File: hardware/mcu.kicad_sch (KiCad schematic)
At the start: 49 parts, among them J10 PRPC006SAAN-RC, J11 SBH11-NBPC-D05-SM-BK, J12 PRPC006SAAN-RC, J13 PRPC006SAAN-RC, J14 PRPC006SAAN-RC, J15 PRPC006SAAN-RC, J16 PRPC006SAAN-RC, J17 PRPC006SAAN-RC, J18 PRPC001DAAN-RC, U7 STM32L552CEU6, U8 AT25SF081B-MAHB-T, Y1 ECS-160-9-37-CKM-TR3, Y2 ABS05-32.768KHZ-9-T

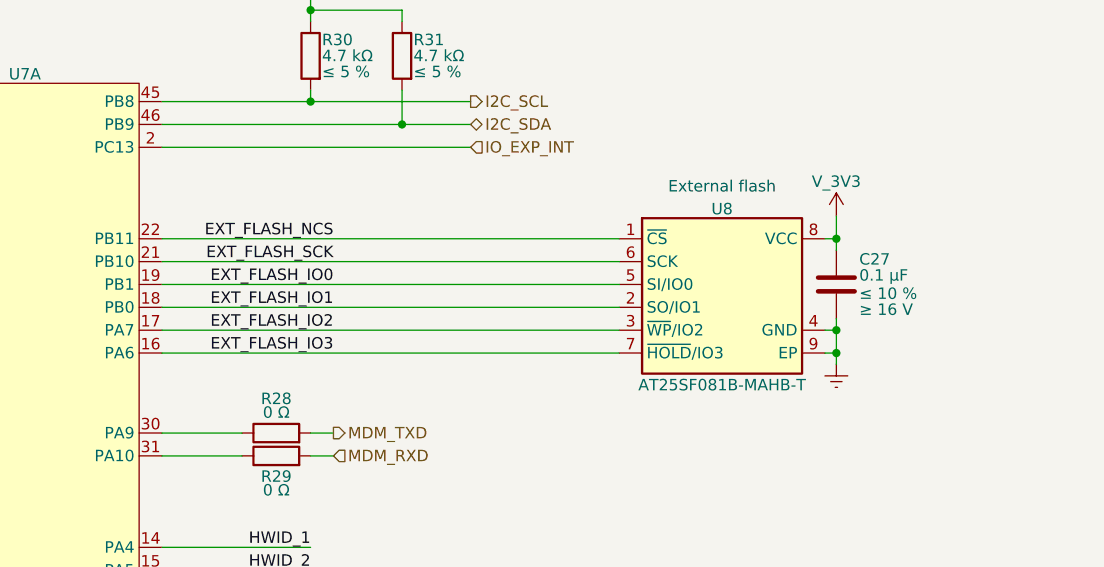
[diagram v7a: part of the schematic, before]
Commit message: HW: Add termination resistors to external flash SPI
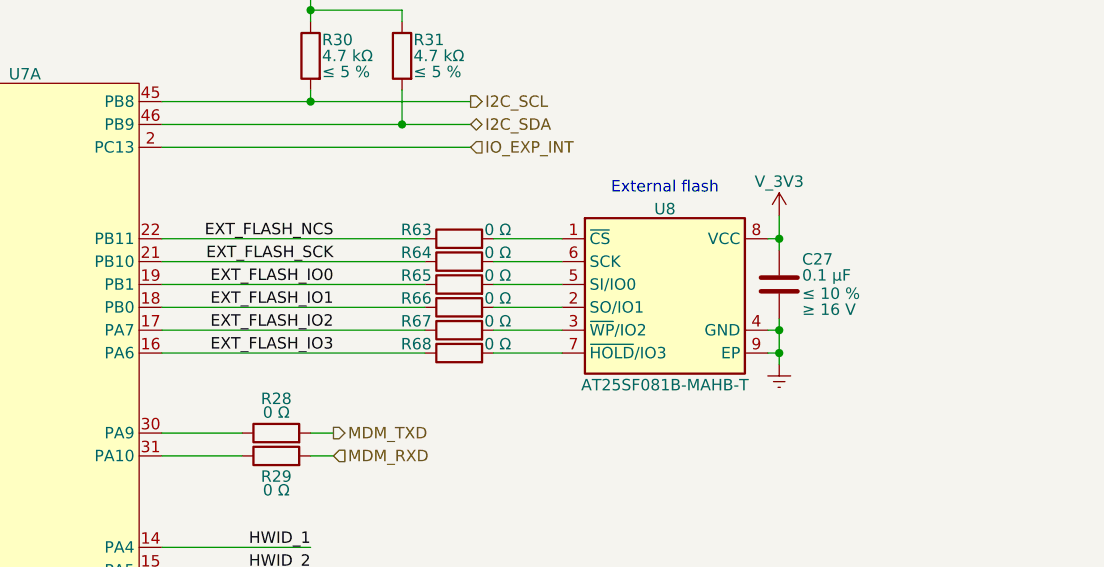
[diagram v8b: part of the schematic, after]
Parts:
- added R63, R64, R65, R66, R67, R68: 0 Ω, Resistor_SMD:R_0402_1005Metric, symbol Device:R
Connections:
- net EXT_FLASH_IO0: now also R65.1; no longer U8.5 (SI/IO0)
- net EXT_FLASH_IO1: now also R66.1; no longer U8.2 (SO/IO1)
- net EXT_FLASH_IO2: now also R67.1; no longer U8.3 (~{WP}/IO2)
- net EXT_FLASH_IO3: now also R68.1; no longer U8.7 (~{HOLD}/IO3)
- net EXT_FLASH_NCS: now also R63.1; no longer U8.1 (~{CS})
- net EXT_FLASH_SCK: now also R64.1; no longer U8.6 (SCK)
- new net: R67.2, U8.3 (~{WP}/IO2)
- new net: R63.2, U8.1 (~{CS})
- new net: R66.2, U8.2 (SO/IO1)
- new net: R65.2, U8.5 (SI/IO0)
- new net: R64.2, U8.6 (SCK)
- new net: R68.2, U8.7 (~{HOLD}/IO3)
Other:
- moved on the sheet: C27, U8
